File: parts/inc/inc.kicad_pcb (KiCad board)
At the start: 2 copper layers, 41.9 x 51.4 mm, 10 parts, among them J1 Conn_02x02_Odd_Even, J2 Conn_02x04_Odd_Even, J3 Conn_01x01, J4 Conn_02x04_Odd_Even, J5 Conn_02x04_Odd_Even, K1 HK19F, K2 HK19F, K3 HK19F, K4 HK19F

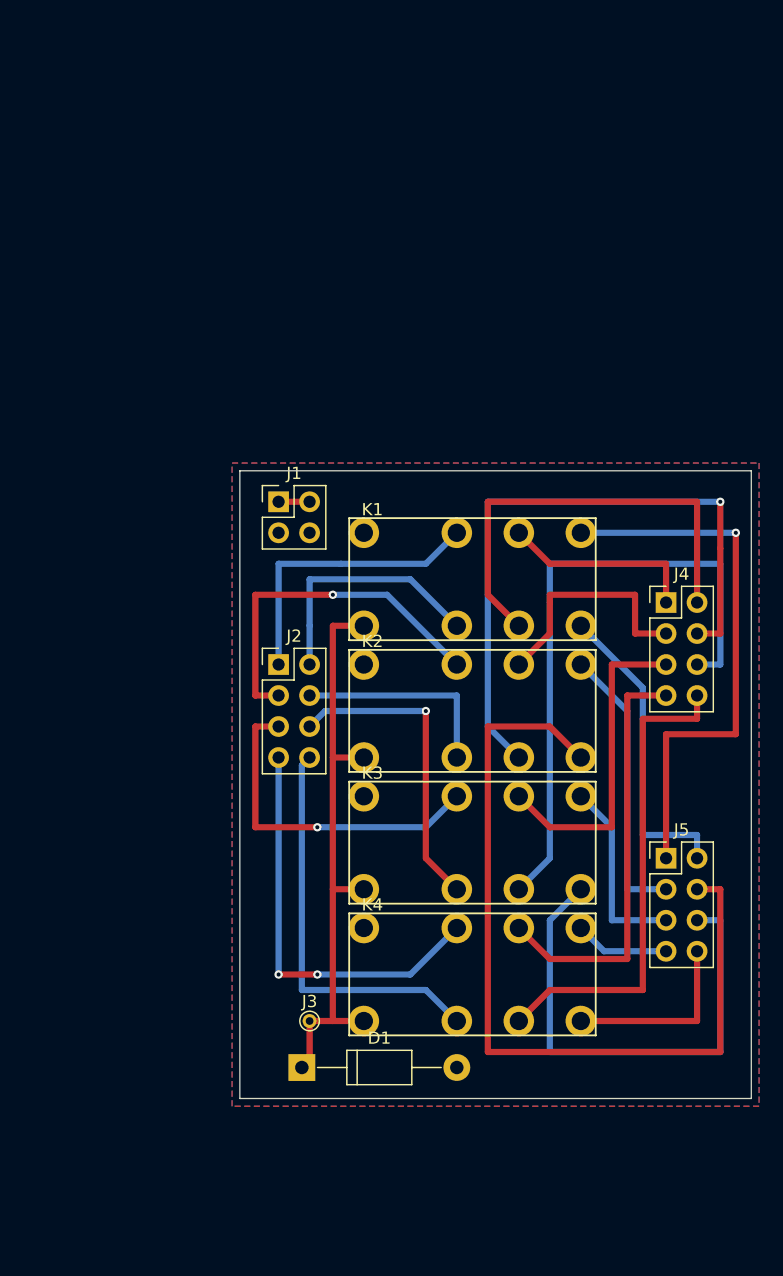
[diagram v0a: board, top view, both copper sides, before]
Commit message: Finish inc (now also with carry out).
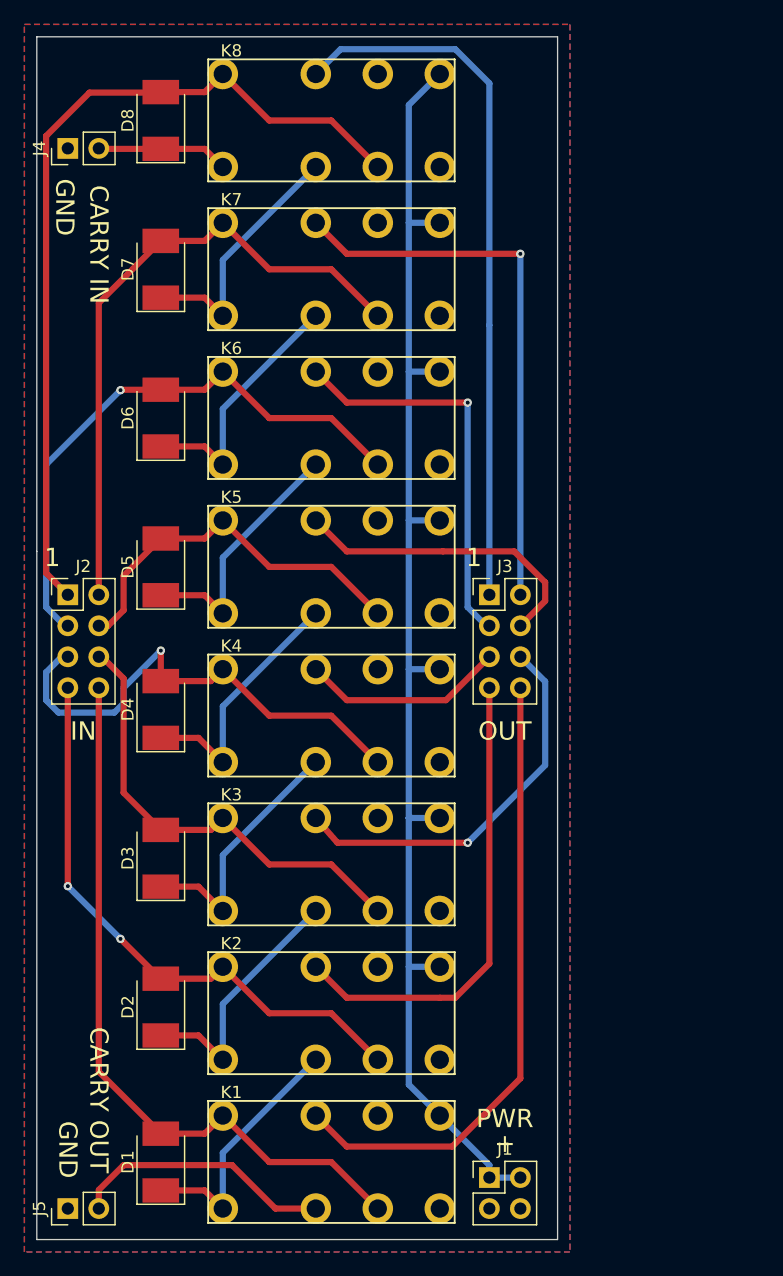
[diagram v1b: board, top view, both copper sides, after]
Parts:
- added D2: D_TVS, Diodes_SMD:D_2114, F.Cu at (150.4, 120.1)
- added D3: D_TVS, Diodes_SMD:D_2114, F.Cu at (150.4, 108.0)
- added D4: D_TVS, Diodes_SMD:D_2114, F.Cu at (150.4, 95.8)
- added D5: D_TVS, Diodes_SMD:D_2114, F.Cu at (150.4, 84.1)
- added D6: D_TVS, Diodes_SMD:D_2114, F.Cu at (150.4, 71.9)
- added D7: D_TVS, Diodes_SMD:D_2114, F.Cu at (150.4, 59.7)
- added D8: D_TVS, Diodes_SMD:D_2114, F.Cu at (150.4, 47.5)
- added K5: HK19F, hk19f:Relay_DPDT_HK19F, F.Cu at (155.4, 80.3)
- added K6: HK19F, hk19f:Relay_DPDT_HK19F, F.Cu at (155.4, 68.1)
- added K7: HK19F, hk19f:Relay_DPDT_HK19F, F.Cu at (155.4, 55.9)
- added K8: HK19F, hk19f:Relay_DPDT_HK19F, F.Cu at (155.4, 43.7)
- D1: value D -> D_TVS; footprint Diodes_THT:D_DO-41_SOD81_P12.70mm_Horizontal -> Diodes_SMD:D_2114
- J3: value Conn_01x01 -> Conn_02x04_Odd_Even; footprint Connectors:PINTST -> Pin_Headers:Pin_Header_Straight_2x04_Pitch2.54mm
- J4, J5: value Conn_02x04_Odd_Even -> Conn_01x02; footprint Pin_Headers:Pin_Header_Straight_2x04_Pitch2.54mm -> Pin_Headers:Pin_Header_Straight_1x02_Pitch2.54mm
- moved J4 61.5 mm to (142.7, 49.8), turned to 90 degrees
- moved J1 58.0 mm to (177.3, 134.1)
- moved J5 56.8 mm to (142.7, 136.7), turned to 90 degrees
- moved K1 49.1 mm to (155.4, 129.0)
- moved J3 37.9 mm to (177.3, 86.4)
- moved K2 27.3 mm to (155.4, 116.8)
- moved K4 24.2 mm to (155.4, 92.5)
- moved J2 18.2 mm to (142.7, 86.4)
- moved D1 13.9 mm to (150.4, 132.8), turned to 90 degrees
- moved K3 11.7 mm to (155.4, 104.6)
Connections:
- D1 pad 2: GND -> Net-(D1-Pad2)
- J2 pad 1: Net-(J2-Pad1) -> Net-(D8-Pad2)
- J2 pad 2: Net-(J2-Pad2) -> Net-(D7-Pad2)
- J2 pad 3: Net-(J2-Pad3) -> Net-(D6-Pad2)
- J2 pad 4: Net-(J2-Pad4) -> Net-(D5-Pad2)
- J2 pad 5: Net-(J2-Pad5) -> Net-(D4-Pad2)
- J2 pad 6: Net-(J2-Pad6) -> Net-(D3-Pad2)
- J2 pad 7: Net-(J2-Pad7) -> Net-(D2-Pad2)
- J2 pad 8: Net-(J2-Pad8) -> Net-(D1-Pad2)
- J3 pad 1: Net-(D1-Pad1) -> Net-(J3-Pad1)
- J4 pad 1: Net-(J4-Pad1) -> GND
- J4 pad 2: Net-(J4-Pad2) -> Net-(D8-Pad1)
- J5 pad 1: Net-(J5-Pad1) -> GND
- K1 pad 1: GND -> Net-(D1-Pad2)
- K1 pad 11: Net-(J4-Pad2) -> Net-(D1-Pad2)
- K1 pad 13: Net-(J2-Pad2) -> Net-(J5-Pad2)
- K1 pad 4: Net-(J2-Pad1) -> Net-(J3-Pad8)
- K1 pad 6: Net-(J4-Pad1) -> GND
- K1 pad 8: Net-(J5-Pad1) -> +12V
- K1 pad 9: Net-(J5-Pad2) -> GND
- K2 pad 1: GND -> Net-(D2-Pad2)
- K2 pad 11: Net-(J4-Pad4) -> Net-(D2-Pad2)
- K2 pad 13: Net-(J2-Pad4) -> Net-(D1-Pad1)
- K2 pad 16: Net-(D1-Pad1) -> Net-(D2-Pad1)
- K2 pad 4: Net-(J2-Pad3) -> Net-(J3-Pad7)
- K2 pad 6: Net-(J4-Pad3) -> GND
- K2 pad 8: Net-(J5-Pad3) -> +12V
- K2 pad 9: Net-(J5-Pad4) -> GND
- K3 pad 1: GND -> Net-(D3-Pad2)
- K3 pad 11: Net-(J4-Pad6) -> Net-(D3-Pad2)
- K3 pad 13: Net-(J2-Pad6) -> Net-(D2-Pad1)
- K3 pad 16: Net-(D1-Pad1) -> Net-(D3-Pad1)
- K3 pad 4: Net-(J2-Pad5) -> Net-(J3-Pad6)
- K3 pad 6: Net-(J4-Pad5) -> GND
- K3 pad 8: Net-(J5-Pad5) -> +12V
- K3 pad 9: Net-(J5-Pad6) -> GND
- K4 pad 1: GND -> Net-(D4-Pad2)
- K4 pad 11: Net-(J4-Pad8) -> Net-(D4-Pad2)
- K4 pad 13: Net-(J2-Pad8) -> Net-(D3-Pad1)
- K4 pad 16: Net-(D1-Pad1) -> Net-(D4-Pad1)
- K4 pad 4: Net-(J2-Pad7) -> Net-(J3-Pad5)
- K4 pad 6: Net-(J4-Pad7) -> GND
- K4 pad 8: Net-(J5-Pad7) -> +12V
- K4 pad 9: Net-(J5-Pad8) -> GND
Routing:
- net +12V: track 2.54 -> 112.5 mm
- net Net-(D8-Pad2): track 0.00 -> 70.8 mm
- net Net-(J5-Pad4): track 69.6 -> 0.00 mm
- net Net-(D1-Pad2): track 0.00 -> 60.2 mm
- net Net-(J3-Pad1): track 0.00 -> 58.1 mm
- net Net-(J4-Pad4): track 53.8 -> 0.00 mm, vias 1 -> 0
- net Net-(D7-Pad2): track 0.00 -> 52.7 mm
- net Net-(J3-Pad8): track 0.00 -> 52.1 mm
- net Net-(J4-Pad6): track 51.9 -> 0.00 mm
- net Net-(D2-Pad2): track 0.00 -> 48.4 mm, vias 0 -> 2
- net Net-(D6-Pad2): track 0.00 -> 47.6 mm, vias 0 -> 1
- net Net-(J3-Pad2): track 0.00 -> 45.8 mm, vias 0 -> 1
- net Net-(J5-Pad1): track 45.1 -> 0.00 mm, vias 1 -> 0
- net Net-(D4-Pad2): track 0.00 -> 41.1 mm, vias 0 -> 1
- net Net-(J5-Pad6): track 41.1 -> 0.00 mm
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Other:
- board size 41.9 x 51.4 mm -> 42.7 x 98.6 mm
- board text added: "+"
- board text added: "1"
- board text added: "CARRY IN"
- board text added: "CARRY OUT"
- board text added: "GND"
- board text added: "IN"
- board text added: "OUT"
- board text added: "PWR"
